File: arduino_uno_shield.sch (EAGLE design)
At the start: 14 parts

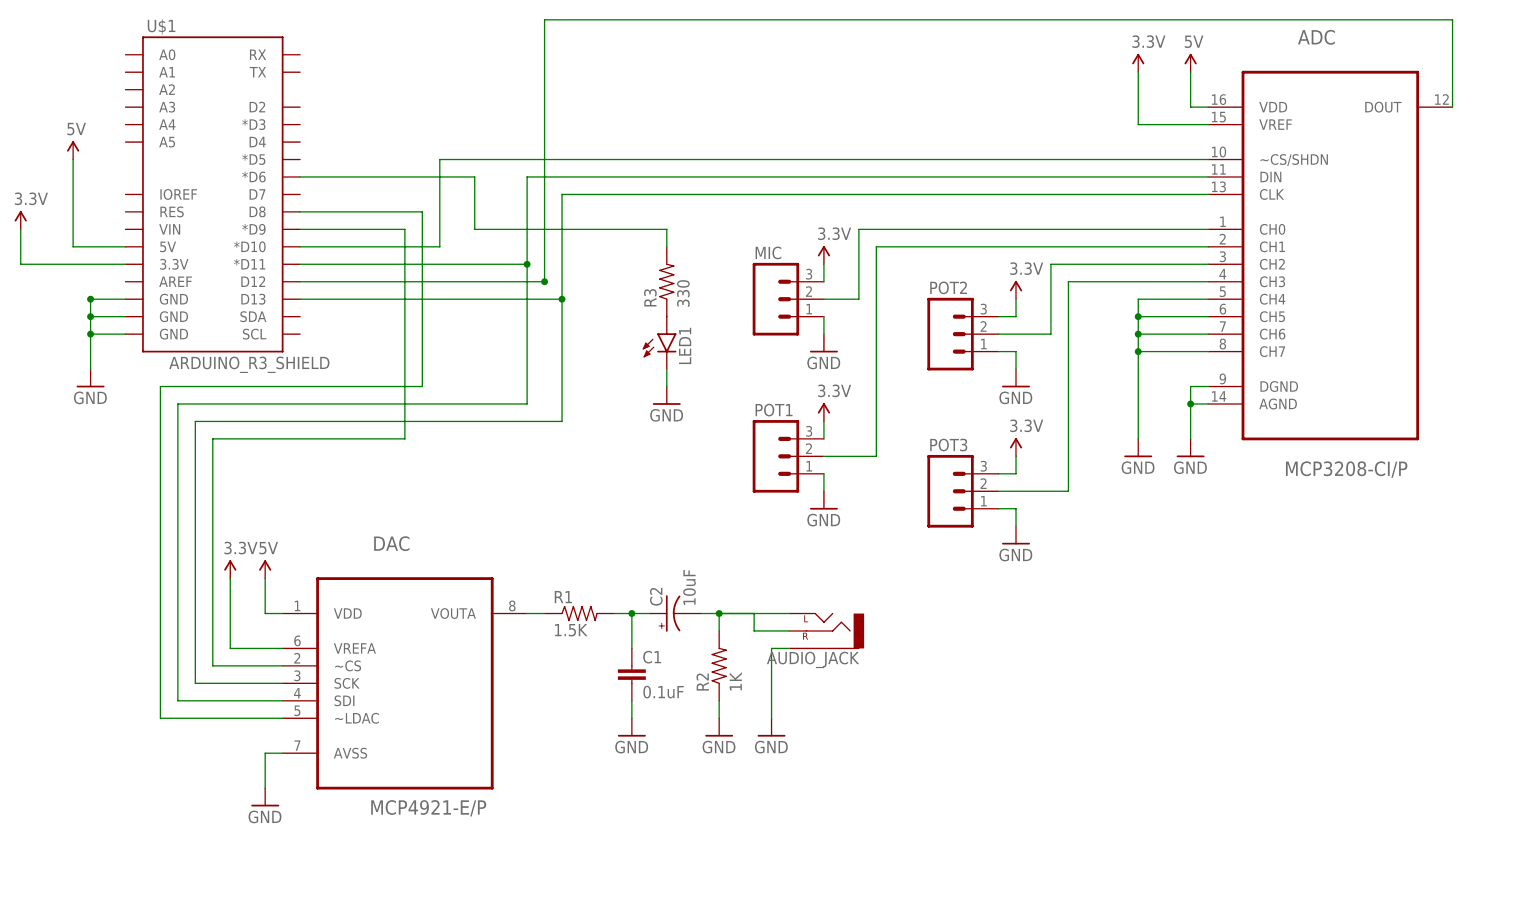
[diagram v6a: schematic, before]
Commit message: clean up board layout
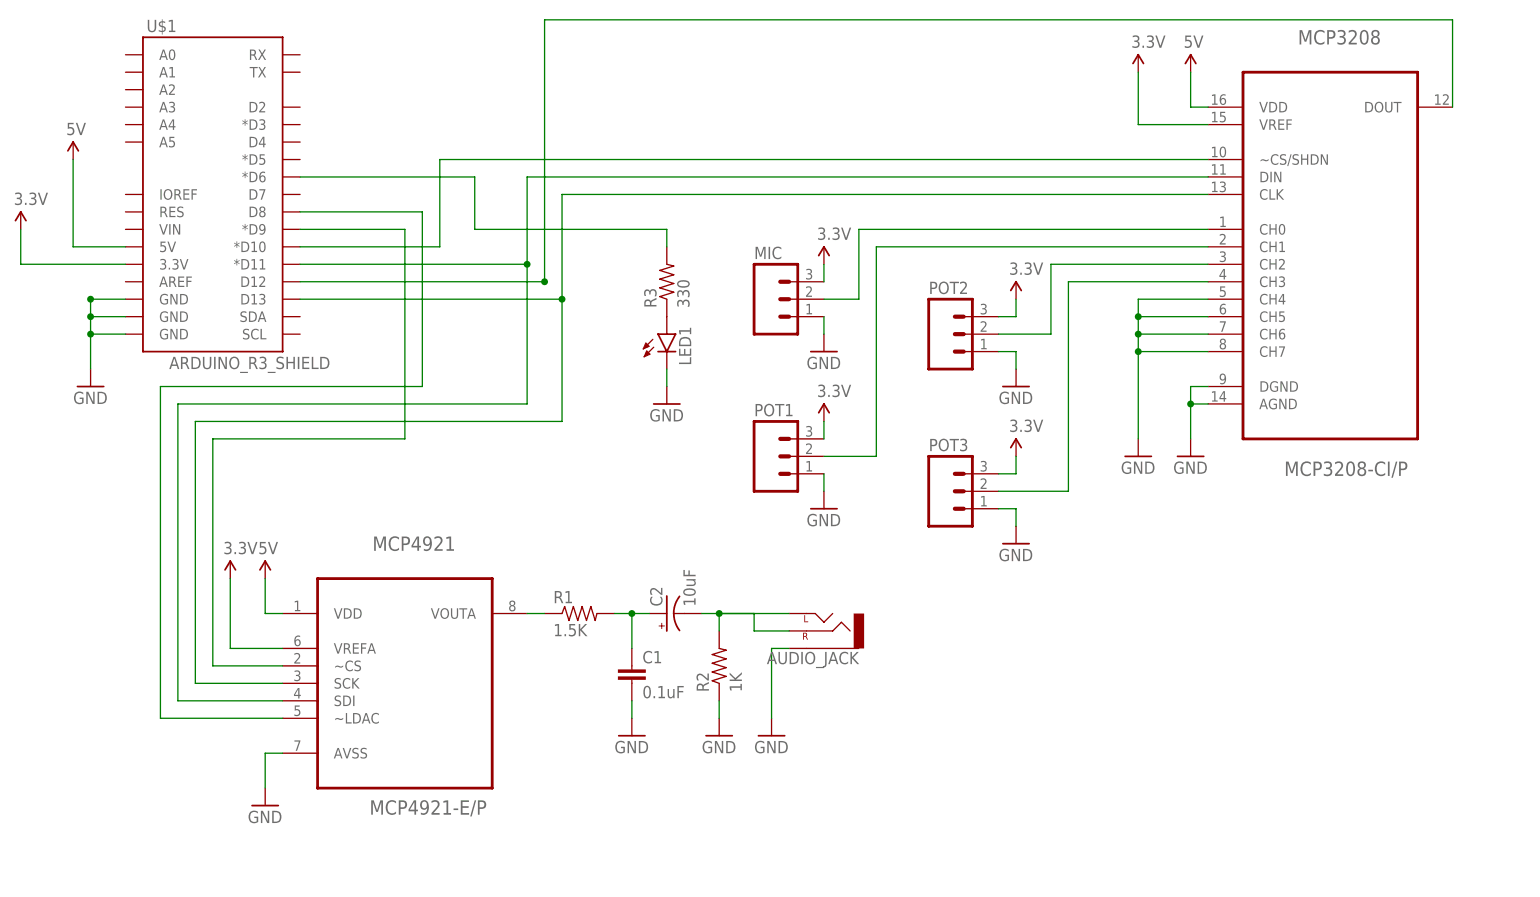
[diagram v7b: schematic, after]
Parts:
- renumbered ADC to MCP3208, DAC to MCP4921
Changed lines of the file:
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@@
 <parts>
 <part name="U$1" library="SparkFun-Boards" deviceset="ARDUINO_R3_SHIELD" device=""/>
-<part name="ADC" library="Microchip_By_element14_Batch_1" deviceset="MCP3208-CI/P" device=""/>
-<part name="DAC" library="Microchip_By_element14_Batch_1" deviceset="MCP4921-E/P" device=""/>
+<part name="MCP3208" library="Microchip_By_element14_Batch_1" deviceset="MCP3208-CI/P" device=""/>
+<part name="MCP4921" library="Microchip_By_element14_Batch_1" deviceset="MCP4921-E/P" device=""/>
 <part name="GND1" library="SparkFun-Aesthetics" deviceset="GND" device=""/>
 <part name="R2" library="SparkFun-Passives" deviceset="RESISTOR" device="PTH-1/4W" value="1K"/>
@@
 <instances>
 <instance part="U$1" gate="G$1" x="-129.54" y="73.66"/>
-<instance part="ADC" gate="A" x="33.02" y="66.04"/>
-<instance part="DAC" gate="A" x="-101.6" y="2.54"/>
+<instance part="MCP3208" gate="A" x="33.02" y="66.04"/>
+<instance part="MCP4921" gate="A" x="-101.6" y="2.54"/>
 <instance part="GND1" gate="1" x="-68.58" y="-7.62"/>
 <instance part="R2" gate="G$1" x="-55.88" y="2.54" rot="R90"/>
@@
 </segment>
 <segment>
-<pinref part="DAC" gate="A" pin="AVSS"/>
+<pinref part="MCP4921" gate="A" pin="AVSS"/>
 <pinref part="GND8" gate="1" pin="GND"/>
 <wire x1="-119.38" y1="-10.16" x2="-121.92" y2="-10.16" width="0.1524" layer="91"/>
@@
 <pinref part="GND2" gate="1" pin="GND"/>
 <wire x1="12.7" y1="35.56" x2="12.7" y2="40.64" width="0.1524" layer="91"/>
-<pinref part="ADC" gate="A" pin="AGND"/>
+<pinref part="MCP3208" gate="A" pin="AGND"/>
 <wire x1="12.7" y1="40.64" x2="15.24" y2="40.64" width="0.1524" layer="91"/>
 <junction x="12.7" y="40.64"/>
 <wire x1="12.7" y1="40.64" x2="12.7" y2="43.18" width="0.1524" layer="91"/>
-<pinref part="ADC" gate="A" pin="DGND"/>
+<pinref part="MCP3208" gate="A" pin="DGND"/>
 <wire x1="12.7" y1="43.18" x2="15.24" y2="43.18" width="0.1524" layer="91"/>
 </segment>
@@
 <pinref part="GND12" gate="1" pin="GND"/>
 <wire x1="5.08" y1="35.56" x2="5.08" y2="48.26" width="0.1524" layer="91"/>
-<pinref part="ADC" gate="A" pin="CH7"/>
+<pinref part="MCP3208" gate="A" pin="CH7"/>
 <wire x1="5.08" y1="48.26" x2="15.24" y2="48.26" width="0.1524" layer="91"/>
 <junction x="5.08" y="48.26"/>
 <wire x1="5.08" y1="48.26" x2="5.08" y2="50.8" width="0.1524" layer="91"/>
-<pinref part="ADC" gate="A" pin="CH6"/>
+<pinref part="MCP3208" gate="A" pin="CH6"/>
 <wire x1="5.08" y1="50.8" x2="15.24" y2="50.8" width="0.1524" layer="91"/>
 <junction x="5.08" y="50.8"/>
 <wire x1="5.08" y1="50.8" x2="5.08" y2="53.34" width="0.1524" layer="91"/>
-<pinref part="ADC" gate="A" pin="CH5"/>
+<pinref part="MCP3208" gate="A" pin="CH5"/>
 <wire x1="5.08" y1="53.34" x2="15.24" y2="53.34" width="0.1524" layer="91"/>
 <junction x="5.08" y="53.34"/>
 <wire x1="5.08" y1="53.34" x2="5.08" y2="55.88" width="0.1524" layer="91"/>
-<pinref part="ADC" gate="A" pin="CH4"/>
+<pinref part="MCP3208" gate="A" pin="CH4"/>
 <wire x1="5.08" y1="55.88" x2="15.24" y2="55.88" width="0.1524" layer="91"/>
 </segment>
@@
 <pinref part="SUPPLY3" gate="G$1" pin="5V"/>
 <wire x1="12.7" y1="88.9" x2="12.7" y2="83.82" width="0.1524" layer="91"/>
-<pinref part="ADC" gate="A" pin="VDD"/>
+<pinref part="MCP3208" gate="A" pin="VDD"/>
 <wire x1="12.7" y1="83.82" x2="15.24" y2="83.82" width="0.1524" layer="91"/>
 </segment>
@@
 <pinref part="SUPPLY4" gate="G$1" pin="5V"/>
 <wire x1="-121.92" y1="15.24" x2="-121.92" y2="10.16" width="0.1524" layer="91"/>
-<pinref part="DAC" gate="A" pin="VDD"/>
+<pinref part="MCP4921" gate="A" pin="VDD"/>
 <wire x1="-121.92" y1="10.16" x2="-119.38" y2="10.16" width="0.1524" layer="91"/>
 </segment>
@@
 <pinref part="SUPPLY6" gate="G$1" pin="3.3V"/>
 <wire x1="5.08" y1="88.9" x2="5.08" y2="81.28" width="0.1524" layer="91"/>
-<pinref part="ADC" gate="A" pin="VREF"/>
+<pinref part="MCP3208" gate="A" pin="VREF"/>
 <wire x1="5.08" y1="81.28" x2="15.24" y2="81.28" width="0.1524" layer="91"/>
 </segment>
@@
 <pinref part="SUPPLY5" gate="G$1" pin="3.3V"/>
 <wire x1="-127" y1="15.24" x2="-127" y2="5.08" width="0.1524" layer="91"/>
-<pinref part="DAC" gate="A" pin="VREFA"/>
+<pinref part="MCP4921" gate="A" pin="VREFA"/>
 <wire x1="-127" y1="5.08" x2="-119.38" y2="5.08" width="0.1524" layer="91"/>
 </segment>
@@
 <net name="N$3" class="0">
 <segment>
-<pinref part="DAC" gate="A" pin="VOUTA"/>
+<pinref part="MCP4921" gate="A" pin="VOUTA"/>
 <pinref part="R1" gate="G$1" pin="1"/>
 <wire x1="-83.82" y1="10.16" x2="-81.28" y2="10.16" width="0.1524" layer="91"/>
@@
 <pinref part="U$1" gate="G$1" pin="D13"/>
 <wire x1="-116.84" y1="55.88" x2="-78.74" y2="55.88" width="0.1524" layer="91"/>
-<pinref part="ADC" gate="A" pin="CLK"/>
+<pinref part="MCP3208" gate="A" pin="CLK"/>
 <wire x1="15.24" y1="71.12" x2="-78.74" y2="71.12" width="0.1524" layer="91"/>
 <wire x1="-78.74" y1="71.12" x2="-78.74" y2="55.88" width="0.1524" layer="91"/>
 <junction x="-78.74" y="55.88"/>
-<pinref part="DAC" gate="A" pin="SCK"/>
+<pinref part="MCP4921" gate="A" pin="SCK"/>
 <wire x1="-119.38" y1="0" x2="-132.08" y2="0" width="0.1524" layer="91"/>
 <wire x1="-132.08" y1="0" x2="-132.08" y2="38.1" width="0.1524" layer="91"/>
@@
 <wire x1="-40.64" y1="55.88" x2="-35.56" y2="55.88" width="0.1524" layer="91"/>
 <wire x1="-35.56" y1="55.88" x2="-35.56" y2="66.04" width="0.1524" layer="91"/>
-<pinref part="ADC" gate="A" pin="CH0"/>
+<pinref part="MCP3208" gate="A" pin="CH0"/>
 <wire x1="-35.56" y1="66.04" x2="15.24" y2="66.04" width="0.1524" layer="91"/>
 </segment>
@@
 <wire x1="-40.64" y1="33.02" x2="-33.02" y2="33.02" width="0.1524" layer="91"/>
 <wire x1="-33.02" y1="33.02" x2="-33.02" y2="63.5" width="0.1524" layer="91"/>
-<pinref part="ADC" gate="A" pin="CH1"/>
+<pinref part="MCP3208" gate="A" pin="CH1"/>
 <wire x1="-33.02" y1="63.5" x2="15.24" y2="63.5" width="0.1524" layer="91"/>
 </segment>
@@
 <wire x1="-116.84" y1="58.42" x2="-81.28" y2="58.42" width="0.1524" layer="91"/>
 <junction x="-81.28" y="58.42"/>
-<pinref part="ADC" gate="A" pin="DOUT"/>
+<pinref part="MCP3208" gate="A" pin="DOUT"/>
 <wire x1="50.8" y1="83.82" x2="50.8" y2="96.52" width="0.1524" layer="91"/>
 <wire x1="50.8" y1="96.52" x2="-81.28" y2="96.52" width="0.1524" layer="91"/>
@@
 <wire x1="-116.84" y1="60.96" x2="-83.82" y2="60.96" width="0.1524" layer="91"/>
 <junction x="-83.82" y="60.96"/>
-<pinref part="ADC" gate="A" pin="DIN"/>
+<pinref part="MCP3208" gate="A" pin="DIN"/>
 <wire x1="15.24" y1="73.66" x2="-83.82" y2="73.66" width="0.1524" layer="91"/>
 <wire x1="-83.82" y1="73.66" x2="-83.82" y2="60.96" width="0.1524" layer="91"/>
@@
 <wire x1="-83.82" y1="40.64" x2="-134.62" y2="40.64" width="0.1524" layer="91"/>
 <wire x1="-134.62" y1="40.64" x2="-134.62" y2="-2.54" width="0.1524" layer="91"/>
-<pinref part="DAC" gate="A" pin="SDI"/>
+<pinref part="MCP4921" gate="A" pin="SDI"/>
 <wire x1="-134.62" y1="-2.54" x2="-119.38" y2="-2.54" width="0.1524" layer="91"/>
 </segment>
@@
 <wire x1="-99.06" y1="43.18" x2="-137.16" y2="43.18" width="0.1524" layer="91"/>
 <wire x1="-137.16" y1="43.18" x2="-137.16" y2="-5.08" width="0.1524" layer="91"/>
-<pinref part="DAC" gate="A" pin="~LDAC"/>
+<pinref part="MCP4921" gate="A" pin="~LDAC"/>
 <wire x1="-137.16" y1="-5.08" x2="-119.38" y2="-5.08" width="0.1524" layer="91"/>
 </segment>
@@
 <net name="N$13" class="0">
 <segment>
-<pinref part="ADC" gate="A" pin="~CS/SHDN"/>
+<pinref part="MCP3208" gate="A" pin="~CS/SHDN"/>
 <wire x1="15.24" y1="76.2" x2="-96.52" y2="76.2" width="0.1524" layer="91"/>
 <wire x1="-96.52" y1="76.2" x2="-96.52" y2="63.5" width="0.1524" layer="91"/>
@@
 <net name="N$5" class="0">
 <segment>
-<pinref part="DAC" gate="A" pin="~CS"/>
+<pinref part="MCP4921" gate="A" pin="~CS"/>
 <wire x1="-119.38" y1="2.54" x2="-129.54" y2="2.54" width="0.1524" layer="91"/>
 <wire x1="-129.54" y1="2.54" x2="-129.54" y2="35.56" width="0.1524" layer="91"/>
@@
 <wire x1="-15.24" y1="50.8" x2="-7.62" y2="50.8" width="0.1524" layer="91"/>
 <wire x1="-7.62" y1="50.8" x2="-7.62" y2="60.96" width="0.1524" layer="91"/>
-<pinref part="ADC" gate="A" pin="CH2"/>
+<pinref part="MCP3208" gate="A" pin="CH2"/>
 <wire x1="-7.62" y1="60.96" x2="15.24" y2="60.96" width="0.1524" layer="91"/>
 </segment>
@@
 <wire x1="-15.24" y1="27.94" x2="-5.08" y2="27.94" width="0.1524" layer="91"/>
 <wire x1="-5.08" y1="27.94" x2="-5.08" y2="58.42" width="0.1524" layer="91"/>
-<pinref part="ADC" gate="A" pin="CH3"/>
+<pinref part="MCP3208" gate="A" pin="CH3"/>
 <wire x1="-5.08" y1="58.42" x2="15.24" y2="58.42" width="0.1524" layer="91"/>
 </segment>

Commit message: add more pot headers
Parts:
- added POT4, POT5, POT6, POT7: (no value), SparkFun-Connectors:M03PTH
- renumbered LED1 to LED
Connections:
- new net N$1: MCP3208.CH4, POT4.2
- new net N$16: MCP3208.CH5, POT5.2
- new net N$17: MCP3208.CH6, POT6.2
- new net N$18: MCP3208.CH7, POT7.2
- net 3.3V: now also POT4.3, POT5.3, POT6.3, POT7.3
- net GND: now also POT4.1, POT5.1, POT6.1, POT7.1; no longer MCP3208.CH4, MCP3208.CH5, MCP3208.CH6, MCP3208.CH7
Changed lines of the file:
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@@
 <part name="MIC" library="SparkFun-Connectors" deviceset="M03" device="PTH"/>
 <part name="POT1" library="SparkFun-Connectors" deviceset="M03" device="PTH"/>
-<part name="LED1" library="SparkFun-LED" deviceset="LED" device="5MM"/>
+<part name="LED" library="SparkFun-LED" deviceset="LED" device="5MM"/>
 <part name="GND3" library="SparkFun-Aesthetics" deviceset="GND" device=""/>
 <part name="SUPPLY3" library="SparkFun-Aesthetics" deviceset="5V" device=""/>
@@
 <part name="SUPPLY12" library="SparkFun-Aesthetics" deviceset="3.3V" device=""/>
 <part name="GND2" library="SparkFun-Aesthetics" deviceset="GND" device=""/>
+<part name="POT4" library="SparkFun-Connectors" deviceset="M03" device="PTH"/>
+<part name="POT5" library="SparkFun-Connectors" deviceset="M03" device="PTH"/>
+<part name="POT6" library="SparkFun-Connectors" deviceset="M03" device="PTH"/>
+<part name="POT7" library="SparkFun-Connectors" deviceset="M03" device="PTH"/>
+<part name="SUPPLY2" library="SparkFun-Aesthetics" deviceset="3.3V" device=""/>
+<part name="SUPPLY10" library="SparkFun-Aesthetics" deviceset="3.3V" device=""/>
+<part name="SUPPLY13" library="SparkFun-Aesthetics" deviceset="3.3V" device=""/>
+<part name="GND13" library="SparkFun-Aesthetics" deviceset="GND" device=""/>
+<part name="GND16" library="SparkFun-Aesthetics" deviceset="GND" device=""/>
+<part name="SUPPLY14" library="SparkFun-Aesthetics" deviceset="3.3V" device=""/>
+<part name="GND17" library="SparkFun-Aesthetics" deviceset="GND" device=""/>
 <part name="GND12" library="SparkFun-Aesthetics" deviceset="GND" device=""/>
 </parts>
@@
 </instance>
 <instance part="POT1" gate="G$1" x="-48.26" y="33.02"/>
-<instance part="LED1" gate="G$1" x="-63.5" y="50.8"/>
+<instance part="LED" gate="G$1" x="-63.5" y="50.8"/>
 <instance part="GND3" gate="1" x="-63.5" y="40.64"/>
 <instance part="SUPPLY3" gate="G$1" x="12.7" y="88.9"/>
@@
 <instance part="SUPPLY12" gate="G$1" x="-12.7" y="55.88"/>
 <instance part="GND2" gate="1" x="12.7" y="33.02"/>
-<instance part="GND12" gate="1" x="5.08" y="33.02"/>
+<instance part="POT4" gate="G$1" x="-22.86" y="5.08"/>
+<instance part="POT5" gate="G$1" x="-22.86" y="-17.78"/>
+<instance part="POT6" gate="G$1" x="35.56" y="17.78" rot="MR0"/>
+<instance part="POT7" gate="G$1" x="35.56" y="-7.62" rot="MR0"/>
+<instance part="SUPPLY2" gate="G$1" x="-12.7" y="10.16"/>
+<instance part="SUPPLY10" gate="G$1" x="-12.7" y="-12.7"/>
+<instance part="SUPPLY13" gate="G$1" x="25.4" y="22.86"/>
+<instance part="GND13" gate="1" x="-12.7" y="-2.54"/>
+<instance part="GND16" gate="1" x="25.4" y="10.16"/>
+<instance part="SUPPLY14" gate="G$1" x="25.4" y="-2.54"/>
+<instance part="GND17" gate="1" x="25.4" y="-15.24"/>
+<instance part="GND12" gate="1" x="-12.7" y="-25.4"/>
 </instances>
 <busses>
@@
 <segment>
 <pinref part="GND3" gate="1" pin="GND"/>
-<pinref part="LED1" gate="G$1" pin="C"/>
+<pinref part="LED" gate="G$1" pin="C"/>
 <wire x1="-63.5" y1="43.18" x2="-63.5" y2="45.72" width="0.1524" layer="91"/>
 </segment>
@@
 </segment>
 <segment>
+<pinref part="POT4" gate="G$1" pin="1"/>
+<wire x1="-15.24" y1="2.54" x2="-12.7" y2="2.54" width="0.1524" layer="91"/>
+<pinref part="GND13" gate="1" pin="GND"/>
+<wire x1="-12.7" y1="2.54" x2="-12.7" y2="0" width="0.1524" layer="91"/>
+</segment>
+<segment>
+<pinref part="POT7" gate="G$1" pin="1"/>
+<wire x1="27.94" y1="-10.16" x2="25.4" y2="-10.16" width="0.1524" layer="91"/>
+<pinref part="GND17" gate="1" pin="GND"/>
+<wire x1="25.4" y1="-10.16" x2="25.4" y2="-12.7" width="0.1524" layer="91"/>
+</segment>
+<segment>
+<pinref part="POT6" gate="G$1" pin="1"/>
+<wire x1="27.94" y1="15.24" x2="25.4" y2="15.24" width="0.1524" layer="91"/>
+<pinref part="GND16" gate="1" pin="GND"/>
+<wire x1="25.4" y1="15.24" x2="25.4" y2="12.7" width="0.1524" layer="91"/>
+</segment>
+<segment>
+<pinref part="POT5" gate="G$1" pin="1"/>
+<wire x1="-15.24" y1="-20.32" x2="-12.7" y2="-20.32" width="0.1524" layer="91"/>
 <pinref part="GND12" gate="1" pin="GND"/>
-<wire x1="5.08" y1="35.56" x2="5.08" y2="48.26" width="0.1524" layer="91"/>
-<pinref part="MCP3208" gate="A" pin="CH7"/>
-<wire x1="5.08" y1="48.26" x2="15.24" y2="48.26" width="0.1524" layer="91"/>
-<junction x="5.08" y="48.26"/>
-<wire x1="5.08" y1="48.26" x2="5.08" y2="50.8" width="0.1524" layer="91"/>
-<pinref part="MCP3208" gate="A" pin="CH6"/>
-<wire x1="5.08" y1="50.8" x2="15.24" y2="50.8" width="0.1524" layer="91"/>
-<junction x="5.08" y="50.8"/>
-<wire x1="5.08" y1="50.8" x2="5.08" y2="53.34" width="0.1524" layer="91"/>
-<pinref part="MCP3208" gate="A" pin="CH5"/>
-<wire x1="5.08" y1="53.34" x2="15.24" y2="53.34" width="0.1524" layer="91"/>
-<junction x="5.08" y="53.34"/>
-<wire x1="5.08" y1="53.34" x2="5.08" y2="55.88" width="0.1524" layer="91"/>
-<pinref part="MCP3208" gate="A" pin="CH4"/>
-<wire x1="5.08" y1="55.88" x2="15.24" y2="55.88" width="0.1524" layer="91"/>
+<wire x1="-12.7" y1="-20.32" x2="-12.7" y2="-22.86" width="0.1524" layer="91"/>
 </segment>
 </net>
@@
 <pinref part="SUPPLY11" gate="G$1" pin="3.3V"/>
 <wire x1="-12.7" y1="30.48" x2="-12.7" y2="33.02" width="0.1524" layer="91"/>
+</segment>
+<segment>
+<pinref part="POT4" gate="G$1" pin="3"/>
+<wire x1="-15.24" y1="7.62" x2="-12.7" y2="7.62" width="0.1524" layer="91"/>
+<pinref part="SUPPLY2" gate="G$1" pin="3.3V"/>
+<wire x1="-12.7" y1="7.62" x2="-12.7" y2="10.16" width="0.1524" layer="91"/>
+</segment>
+<segment>
+<pinref part="POT5" gate="G$1" pin="3"/>
+<wire x1="-15.24" y1="-15.24" x2="-12.7" y2="-15.24" width="0.1524" layer="91"/>
+<pinref part="SUPPLY10" gate="G$1" pin="3.3V"/>
+<wire x1="-12.7" y1="-15.24" x2="-12.7" y2="-12.7" width="0.1524" layer="91"/>
+</segment>
+<segment>
+<pinref part="POT7" gate="G$1" pin="3"/>
+<wire x1="27.94" y1="-5.08" x2="25.4" y2="-5.08" width="0.1524" layer="91"/>
+<pinref part="SUPPLY14" gate="G$1" pin="3.3V"/>
+<wire x1="25.4" y1="-5.08" x2="25.4" y2="-2.54" width="0.1524" layer="91"/>
+</segment>
+<segment>
+<pinref part="POT6" gate="G$1" pin="3"/>
+<wire x1="27.94" y1="20.32" x2="25.4" y2="20.32" width="0.1524" layer="91"/>
+<pinref part="SUPPLY13" gate="G$1" pin="3.3V"/>
+<wire x1="25.4" y1="20.32" x2="25.4" y2="22.86" width="0.1524" layer="91"/>
 </segment>
 </net>
@@
 <net name="N$10" class="0">
 <segment>
-<pinref part="LED1" gate="G$1" pin="A"/>
+<pinref part="LED" gate="G$1" pin="A"/>
 <pinref part="R3" gate="G$1" pin="1"/>
 </segment>
@@
 </segment>
 </net>
+<net name="N$1" class="0">
+<segment>
+<pinref part="MCP3208" gate="A" pin="CH4"/>
+<wire x1="15.24" y1="55.88" x2="-2.54" y2="55.88" width="0.1524" layer="91"/>
+<wire x1="-2.54" y1="55.88" x2="-2.54" y2="5.08" width="0.1524" layer="91"/>
+<pinref part="POT4" gate="G$1" pin="2"/>
+<wire x1="-2.54" y1="5.08" x2="-15.24" y2="5.08" width="0.1524" layer="91"/>
+</segment>
+</net>
+<net name="N$16" class="0">
+<segment>
+<pinref part="MCP3208" gate="A" pin="CH5"/>
+<wire x1="15.24" y1="53.34" x2="0" y2="53.34" width="0.1524" layer="91"/>
+<wire x1="0" y1="53.34" x2="0" y2="-17.78" width="0.1524" layer="91"/>
+<pinref part="POT5" gate="G$1" pin="2"/>
+<wire x1="0" y1="-17.78" x2="-15.24" y2="-17.78" width="0.1524" layer="91"/>
+</segment>
+</net>
+<net name="N$17" class="0">
+<segment>
+<pinref part="MCP3208" gate="A" pin="CH6"/>
+<wire x1="15.24" y1="50.8" x2="7.62" y2="50.8" width="0.1524" layer="91"/>
+<wire x1="7.62" y1="50.8" x2="7.62" y2="17.78" width="0.1524" layer="91"/>
+<pinref part="POT6" gate="G$1" pin="2"/>
+<wire x1="7.62" y1="17.78" x2="27.94" y2="17.78" width="0.1524" layer="91"/>
+</segment>
+</net>
+<net name="N$18" class="0">
+<segment>
+<pinref part="MCP3208" gate="A" pin="CH7"/>
+<wire x1="15.24" y1="48.26" x2="5.08" y2="48.26" width="0.1524" layer="91"/>
+<wire x1="5.08" y1="48.26" x2="5.08" y2="-7.62" width="0.1524" layer="91"/>
+<pinref part="POT7" gate="G$1" pin="2"/>
+<wire x1="5.08" y1="-7.62" x2="27.94" y2="-7.62" width="0.1524" layer="91"/>
+</segment>
+</net>
